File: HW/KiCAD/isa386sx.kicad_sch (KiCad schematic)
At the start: 174 parts, among them CON1 CF-CARD-cfcard, J10 PC104_16, J11 PC104, J12 USB_B, J13 POWER 5V2A, J14 COM1, J15 COM2, J16 ESP, J17 Mini-DIN-6, J18 Mini-DIN-6, J9 Conn_01x04, Q1 BC817, Q2 BC856, Q3 BC856, SW1 Jumper / Pin header 1x2 Pitch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, SW2 SW_Push, SW3 SW_DIP_x01, U10 74HCT32PW, U11 MSM5118160F-JS, U12 74HCT138PW, U13 ST16C554D, U14 74HCT138PW, U15 GD75232PW, U16 GD75232PW, U17 MAX809LEUR, U18 CH340G, U19 LMR62014, U20 ESP-12F, U21 IP4220CZ6, U22 IP4220CZ6, U23 1117-3.3, U24 ICL7660A, U25 39SF040, U26 TXS0104PW, U6 MSM5118160F-JS, U7 M6117D, U8 MSM5118160F-JS, U9 MSM5118160F-JS, X1 14.318 MHz, X2 80 MHz, X3 1.8432 Mhz, Y3 32768 Hz, Y4 12 MHz

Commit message: some edit
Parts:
- BT1: footprint my:CR2032V -> Battery:BatteryHolder_MYOUNG_BS-07-A1BJ001_CR2032
- C102, C103, C98: footprint Capacitor_Tantalum_SMD:CP_EIA-3528-21_Kemet-B_Pad1.50x2.35mm_HandSolder -> Capacitor_Tantalum_SMD:CP_EIA-3528-21_Kemet-B_HandSolder
- C75: footprint Capacitor_Tantalum_SMD:CP_EIA-7343-31_Kemet-D_Pad2.25x2.55mm_HandSolder -> Capacitor_Tantalum_SMD:CP_EIA-7343-31_Kemet-D_HandSolder
- CON1: footprint my:TE_1734451-1-LONG -> Library:TE_1734451-1
- H1, H2, H3, H4: footprint my:MountingHole_3.2mm_M3_dk5.2mm_Mask -> Library_user:MountingHole_3.2mm_M3_dk5.2mm_Mask
- J17, J18: footprint my:minidin-6 -> Library_user:minidin-6
- LOGO1: footprint mygraphic:black-mage-12.5x8.6 -> Library_user:black-mage-12.5x8.6
- U11, U6, U8, U9: footprint my:SOJ-42 -> Library_user:SOJ-42
- U25: footprint my:PLCC-32_11.4x14.0mm_P1.27mm-longpads -> Library_user:PLCC-32_11.4x14.0mm_P1.27mm-longpads
- X1, X2: footprint my:Oscillator_SMD_7050_7.0x5.0mm -> Oscillator:Oscillator_SMD_Abracon_ASE-4Pin_3.2x2.5mm_HandSoldering
- X3: footprint my:Oscillator_SMD_7050_7.0x5.0mm -> Oscillator:Oscillator_SMD_Abracon_ASV-4Pin_7.0x5.1mm_HandSoldering
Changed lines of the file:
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@@
 			)
 		)
-		(property "Footprint" "my:TE_1734451-1-LONG"
+		(property "Footprint" "Library:TE_1734451-1"
 			(at 233.172 69.85 0)
 			(effects
@@
 			)
 		)
-		(property "Footprint" "my:PLCC-32_11.4x14.0mm_P1.27mm-longpads"
+		(property "Footprint" "Library_user:PLCC-32_11.4x14.0mm_P1.27mm-longpads"
 			(at 542.29 236.22 0)
 			(effects
@@
 			)
 		)
-		(property "Footprint" "Capacitor_Tantalum_SMD:CP_EIA-7343-31_Kemet-D_Pad2.25x2.55mm_HandSolder"
+		(property "Footprint" "Capacitor_Tantalum_SMD:CP_EIA-7343-31_Kemet-D_HandSolder"
 			(at 411.1752 -17.78 0)
 			(effects
@@
 			)
 		)
-		(property "Footprint" "my:CR2032V"
+		(property "Footprint" "Battery:BatteryHolder_MYOUNG_BS-07-A1BJ001_CR2032"
 			(at 566.42 40.386 90)
 			(effects
@@
 			)
 		)
-		(property "Footprint" "my:SOJ-42"
+		(property "Footprint" "Library_user:SOJ-42"
 			(at 137.16 358.14 0)
 			(effects
@@
 			)
 		)
-		(property "Footprint" "my:MountingHole_3.2mm_M3_dk5.2mm_Mask"
+		(property "Footprint" "Library_user:MountingHole_3.2mm_M3_dk5.2mm_Mask"
 			(at 552.45 293.37 0)
 			(effects
@@
 			)
 		)
-		(property "Footprint" "my:MountingHole_3.2mm_M3_dk5.2mm_Mask"
+		(property "Footprint" "Library_user:MountingHole_3.2mm_M3_dk5.2mm_Mask"
 			(at 552.45 298.45 0)
 			(effects
@@
 			)
 		)
-		(property "Footprint" "my:MountingHole_3.2mm_M3_dk5.2mm_Mask"
+		(property "Footprint" "Library_user:MountingHole_3.2mm_M3_dk5.2mm_Mask"
 			(at 552.45 303.53 0)
 			(effects
@@
 			)
 		)
-		(property "Footprint" "my:Oscillator_SMD_7050_7.0x5.0mm"
+		(property "Footprint" "Oscillator:Oscillator_SMD_Abracon_ASE-4Pin_3.2x2.5mm_HandSoldering"
 			(at 233.68 223.52 0)
 			(effects
@@
 			)
 		)
-		(property "Footprint" "Capacitor_Tantalum_SMD:CP_EIA-3528-21_Kemet-B_Pad1.50x2.35mm_HandSolder"
+		(property "Footprint" "Capacitor_Tantalum_SMD:CP_EIA-3528-21_Kemet-B_HandSolder"
 			(at 563.5752 90.17 0)
 			(effects
@@
 			)
 		)
-		(property "Footprint" "my:minidin-6"
+		(property "Footprint" "Library_user:minidin-6"
 			(at 560.07 171.45 0)
 			(effects
@@
 			)
 		)
-		(property "Footprint" "my:minidin-6"
+		(property "Footprint" "Library_user:minidin-6"
 			(at 560.07 133.35 0)
 			(effects
@@
 			)
 		)
-		(property "Footprint" "Capacitor_Tantalum_SMD:CP_EIA-3528-21_Kemet-B_Pad1.50x2.35mm_HandSolder"
+		(property "Footprint" "Capacitor_Tantalum_SMD:CP_EIA-3528-21_Kemet-B_HandSolder"
 			(at 540.7152 39.37 0)
 			(effects
@@
 			)
 		)
-		(property "Footprint" "my:MountingHole_3.2mm_M3_dk5.2mm_Mask"
+		(property "Footprint" "Library_user:MountingHole_3.2mm_M3_dk5.2mm_Mask"
 			(at 552.45 288.29 0)
 			(effects
@@
 			)
 		)
-		(property "Footprint" "my:Oscillator_SMD_7050_7.0x5.0mm"
+		(property "Footprint" "Oscillator:Oscillator_SMD_Abracon_ASE-4Pin_3.2x2.5mm_HandSoldering"
 			(at 233.68 199.39 0)
 			(effects
@@
 			)
 		)
-		(property "Footprint" "my:SOJ-42"
+		(property "Footprint" "Library_user:SOJ-42"
 			(at 260.35 358.14 0)
 			(effects
@@
 			)
 		)
-		(property "Footprint" "my:SOJ-42"
+		(property "Footprint" "Library_user:SOJ-42"
 			(at 73.66 358.14 0)
 			(effects
@@
 			)
 		)
-		(property "Footprint" "Capacitor_Tantalum_SMD:CP_EIA-3528-21_Kemet-B_Pad1.50x2.35mm_HandSolder"
+		(property "Footprint" "Capacitor_Tantalum_SMD:CP_EIA-3528-21_Kemet-B_HandSolder"
 			(at 555.9552 97.79 0)
 			(effects
@@
 			)
 		)
-		(property "Footprint" "my:Oscillator_SMD_7050_7.0x5.0mm"
+		(property "Footprint" "Oscillator:Oscillator_SMD_Abracon_ASV-4Pin_7.0x5.1mm_HandSoldering"
 			(at 309.88 276.86 0)
 			(effects
@@
 			)
 		)
-		(property "Footprint" "my:SOJ-42"
+		(property "Footprint" "Library_user:SOJ-42"
 			(at 196.85 358.14 0)
 			(effects
@@
 			)
 		)
-		(property "Footprint" "mygraphic:black-mage-12.5x8.6"
+		(property "Footprint" "Library_user:black-mage-12.5x8.6"
 			(at 523.24 301.625 0)
 			(effects

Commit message: pcb edit
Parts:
- removed RN1, RN2, RN3, RN4: 4.7k, Resistor_SMD:R_Array_Convex_4x0603, symbol Device:R_Pack04
- removed RN5, RN6: 330, Resistor_SMD:R_Array_Convex_4x0603, symbol Device:R_Pack04
- removed RN7: 1k, Resistor_SMD:R_Array_Convex_4x0603, symbol Device:R_Pack04
- added R100, R101, R102, R103, R104, R105, R106, R107, R108, R109, R110, R111, R112, R113, R114, R115, R116, R117, R88, R93, R94, R95, R96, R97, R98, R99: 4.7k, Resistor_SMD:R_0805_2012Metric_Pad1.20x1.40mm_HandSolder, symbol Device:R
- C100, C101, C29, C30, C31, C33, C34, C35, C36, C37, C38, C39, C40, C41, C42, C43, C44, C45, C46, C47, C48, C49, C50, C51, C52, C53, C54, C55, C56, C57, C58, C59, C60, C61, C62, C63, C64, C65, C66, C67, C68, C69, C71, C73, C76, C77, C79, C80, C81, C82, C83, C85, C86, C87, C88, C90, C91, C92, C96, C97, C99: footprint Capacitor_SMD:C_0603_1608Metric_Pad1.08x0.95mm_HandSolder -> Capacitor_SMD:C_0805_2012Metric_Pad1.18x1.45mm_HandSolder
- L4: footprint Inductor_SMD:L_Taiyo-Yuden_NR-60xx_HandSoldering -> Inductor_SMD:L_Panasonic_PCC-M0850M
- R24, R25, R26, R27, R28, R29, R31, R32, R33, R34, R35, R36, R37, R38, R39, R40, R43, R44, R45, R46, R47, R48, R49, R50, R51, R52: footprint Resistor_SMD:R_0603_1608Metric_Pad0.98x0.95mm_HandSolder -> Resistor_SMD:R_0805_2012Metric_Pad1.20x1.40mm_HandSolder
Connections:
- net +5V: now also R100.2, R101.2, R102.2, R103.2, R104.2, R105.2, R106.2, R107.2, R108.2, R109.2, R110.2, R111.2, R112.2, R113.2, R114.2, R115.2, R116.2, R117.2, R96.2, R97.2, R98.2, R99.2
- net GND: now also R88.1, R93.1, R94.1, R95.1
- net IOCS16: now also R111.1
- net ISA_AEN: now also R104.1
- net ISA_DACK0: now also R93.2
- net ISA_DACK1: now also R94.2
- net ISA_DACK5: now also R95.2
- net ISA_IOCHK: now also R117.1
- net ISA_IOR: now also R115.1
- net ISA_IORDY: now also R108.1
- net ISA_IOW: now also R114.1
- net ISA_MASTER: now also R110.1
- net ISA_MEMCS16: now also R116.1
- net ISA_MEMR: now also R105.1
- net ISA_MEMW: now also R106.1
- net ISA_NOWS: now also R107.1
- net ISA_REFRESH: now also R109.1
- net ISA_SD0: now also R103.1
- net ISA_SD1: now also R102.1
- net ISA_SD2: now also R101.1
- net ISA_SD3: now also R100.1
- net ISA_SD4: now also R99.1
- net ISA_SD5: now also R98.1
- net ISA_SD6: now also R97.1
- net ISA_SD7: now also R96.1
- net ISA_SMEMR: now also R113.1
- net ISA_SMEMW: now also R112.1
- net ISA_TC: now also R88.2
- no-connect marks 80 -> 78

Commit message: some eidts, remove com
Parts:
- removed C88, C91: 22p, Capacitor_SMD:C_0805_2012Metric_Pad1.18x1.45mm_HandSolder, symbol Device:C
- removed C90: 10n, Capacitor_SMD:C_0805_2012Metric_Pad1.18x1.45mm_HandSolder, symbol Device:C
- removed J14: COM1, Connector_PinHeader_2.54mm:PinHeader_2x05_P2.54mm_Vertical, symbol Connector_Generic:Conn_02x05_Odd_Even
- removed J15: COM2, Connector_PinHeader_2.54mm:PinHeader_2x05_P2.54mm_Vertical, symbol Connector_Generic:Conn_02x05_Odd_Even
- removed J16: ESP, Connector_PinHeader_2.54mm:PinHeader_2x05_P2.54mm_Vertical, symbol Connector_Generic:Conn_02x05_Odd_Even
- removed R41, R42: 22, Resistor_SMD:R_0805_2012Metric_Pad1.20x1.40mm_HandSolder, symbol Device:R
- removed R45, R46: 10k, Resistor_SMD:R_0805_2012Metric_Pad1.20x1.40mm_HandSolder, symbol Device:R
- removed unit 4 of U10
- removed unit 3 of U10
- removed U12, U14: 74HCT138PW, Package_SO:TSSOP-16_4.4x5mm_P0.65mm, symbol 74xx:74LS138
- removed U13: ST16C554D, Package_QFP:LQFP-64_10x10mm_P0.5mm, symbol my:ST16C554-LQFP
- removed U15, U16: GD75232PW, Package_SO:TSSOP-20_4.4x6.5mm_P0.65mm, symbol Interface_UART:GD75232PW
- removed U18: CH340G, Package_SO:SOIC-16_3.9x9.9mm_P1.27mm, symbol Interface_USB:CH340G
- removed U20: ESP-12F, RF_Module:ESP-12E, symbol RF_Module:ESP-12E
- removed U26: TXS0104PW, Package_SO:TSSOP-14_4.4x5mm_P0.65mm, symbol Logic_LevelTranslator:TXB0104PW
- removed X3: 1.8432 Mhz, Oscillator:Oscillator_SMD_Abracon_ASV-4Pin_7.0x5.1mm_HandSoldering, symbol Oscillator:XO91
- removed Y4: 12 MHz, Crystal:Crystal_SMD_SeikoEpson_TSX3225-4Pin_3.2x2.5mm_HandSoldering, symbol Device:Crystal_GND24
- C100: renamed from C103; footprint Capacitor_Tantalum_SMD:CP_EIA-3528-21_Kemet-B_HandSolder -> Capacitor_Tantalum_SMD:CP_EIA-3528-21_Kemet-B_Pad1.50x2.35mm_HandSolder
- C96: renamed from C75; footprint Capacitor_Tantalum_SMD:CP_EIA-7343-31_Kemet-D_HandSolder -> Capacitor_Tantalum_SMD:CP_EIA-7343-31_Kemet-D_Pad2.25x2.55mm_HandSolder
- C97: renamed from C98; footprint Capacitor_Tantalum_SMD:CP_EIA-3528-21_Kemet-B_HandSolder -> Capacitor_Tantalum_SMD:CP_EIA-7343-31_Kemet-D_Pad2.25x2.55mm_HandSolder
- C99: renamed from C102; footprint Capacitor_Tantalum_SMD:CP_EIA-3528-21_Kemet-B_HandSolder -> Capacitor_Tantalum_SMD:CP_EIA-3528-21_Kemet-B_Pad1.50x2.35mm_HandSolder
- CON1: footprint Library:TE_1734451-1 -> Library_user:TE_1734451-1-LONG
- L4: footprint Inductor_SMD:L_Panasonic_PCC-M0850M -> Inductor_SMD:L_7.3x7.3_H4.5
- renumbered C87 to C32, C96 to C36, C97 to C37, C36 to C38, C37 to C39, C38 to C40, C99 to C41, C100 to C42, C39 to C43, C40 to C44, C41 to C45, C42 to C46, C43 to C47, C44 to C48, C45 to C49, C46 to C50, C47 to C51, C48 to C52, C49 to C53, C50 to C54, C51 to C55, C52 to C56, C53 to C57, C54 to C58, C55 to C59, C56 to C60, C57 to C61, C58 to C62, C59 to C63, C60 to C64, C61 to C65, C62 to C66, C63 to C67, C64 to C68, C65 to C69, C66 to C70, C32 to C71, C67 to C72, C68 to C73, C69 to C74, C70 to C75, C71 to C76, C72 to C77, C73 to C78, C74 to C79, C76 to C80, C77 to C81, C78 to C82, C79 to C83, C80 to C84, C81 to C85, C82 to C86, C83 to C87, C84 to C88, C85 to C89, C86 to C90, C89 to C91, C101 to C98, D6 to D4, D7 to D5, D8 to D6, D4 to D7, D5 to D8, J17 to J11, J18 to J12, J11 to J13, J12 to J14, J13 to J15, Q3 to Q2, Q2 to Q3, R88 to R25, R93 to R26, R94 to R27, R95 to R28, R25 to R29, R26 to R30, R27 to R31, R28 to R32, R96 to R33, R97 to R34, R98 to R35, R99 to R36, R100 to R37, R101 to R38, R102 to R39, R103 to R40, R104 to R41, R105 to R42, R106 to R43, R107 to R44, R108 to R45, R109 to R46, R110 to R47, R111 to R48, R112 to R49, R113 to R50, R114 to R51, R115 to R52, R116 to R53, R117 to R54, R29 to R55, R30 to R56, R38 to R57, R31 to R58, R40 to R59, R48 to R60, R49 to R61, R50 to R62, R51 to R63, R52 to R64, R32 to R65, R34 to R66, R35 to R67, R36 to R68, R39 to R69, R43 to R70, R44 to R71, R33 to R72, R47 to R73, R37 to R74, SW2 to SW1, SW3 to SW2, SW1 to SW3, U17 to U11, U11 to U12, U21 to U13, U22 to U14, U25 to U15, U19 to U16, U23 to U17, U24 to U18
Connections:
- no-connect marks 78 -> 51
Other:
- note removed: "19mA"
- note removed: "215mA"
- note removed: "30mA"
- note removed: "6mA"
- note removed: "COM (UART)"
- note removed: "COM1 (C): I/O port 0x3F8, IRQ 4 COM2 (D): I/O port 0x2F8, IRQ 3 COM3 (B): I/O port 0x3E8, IRQ 4 - USB COM4 (A): I/O port 0x2E8, IRQ 3 - WiFi"
- note removed: "Pull ESP_BOOT to GND to enter programming mode."
- note removed: "WiFi"
- moved on the sheet: C32, C36, C37, C41, C42, C71, C96, D1, D2, D3, D7, D8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

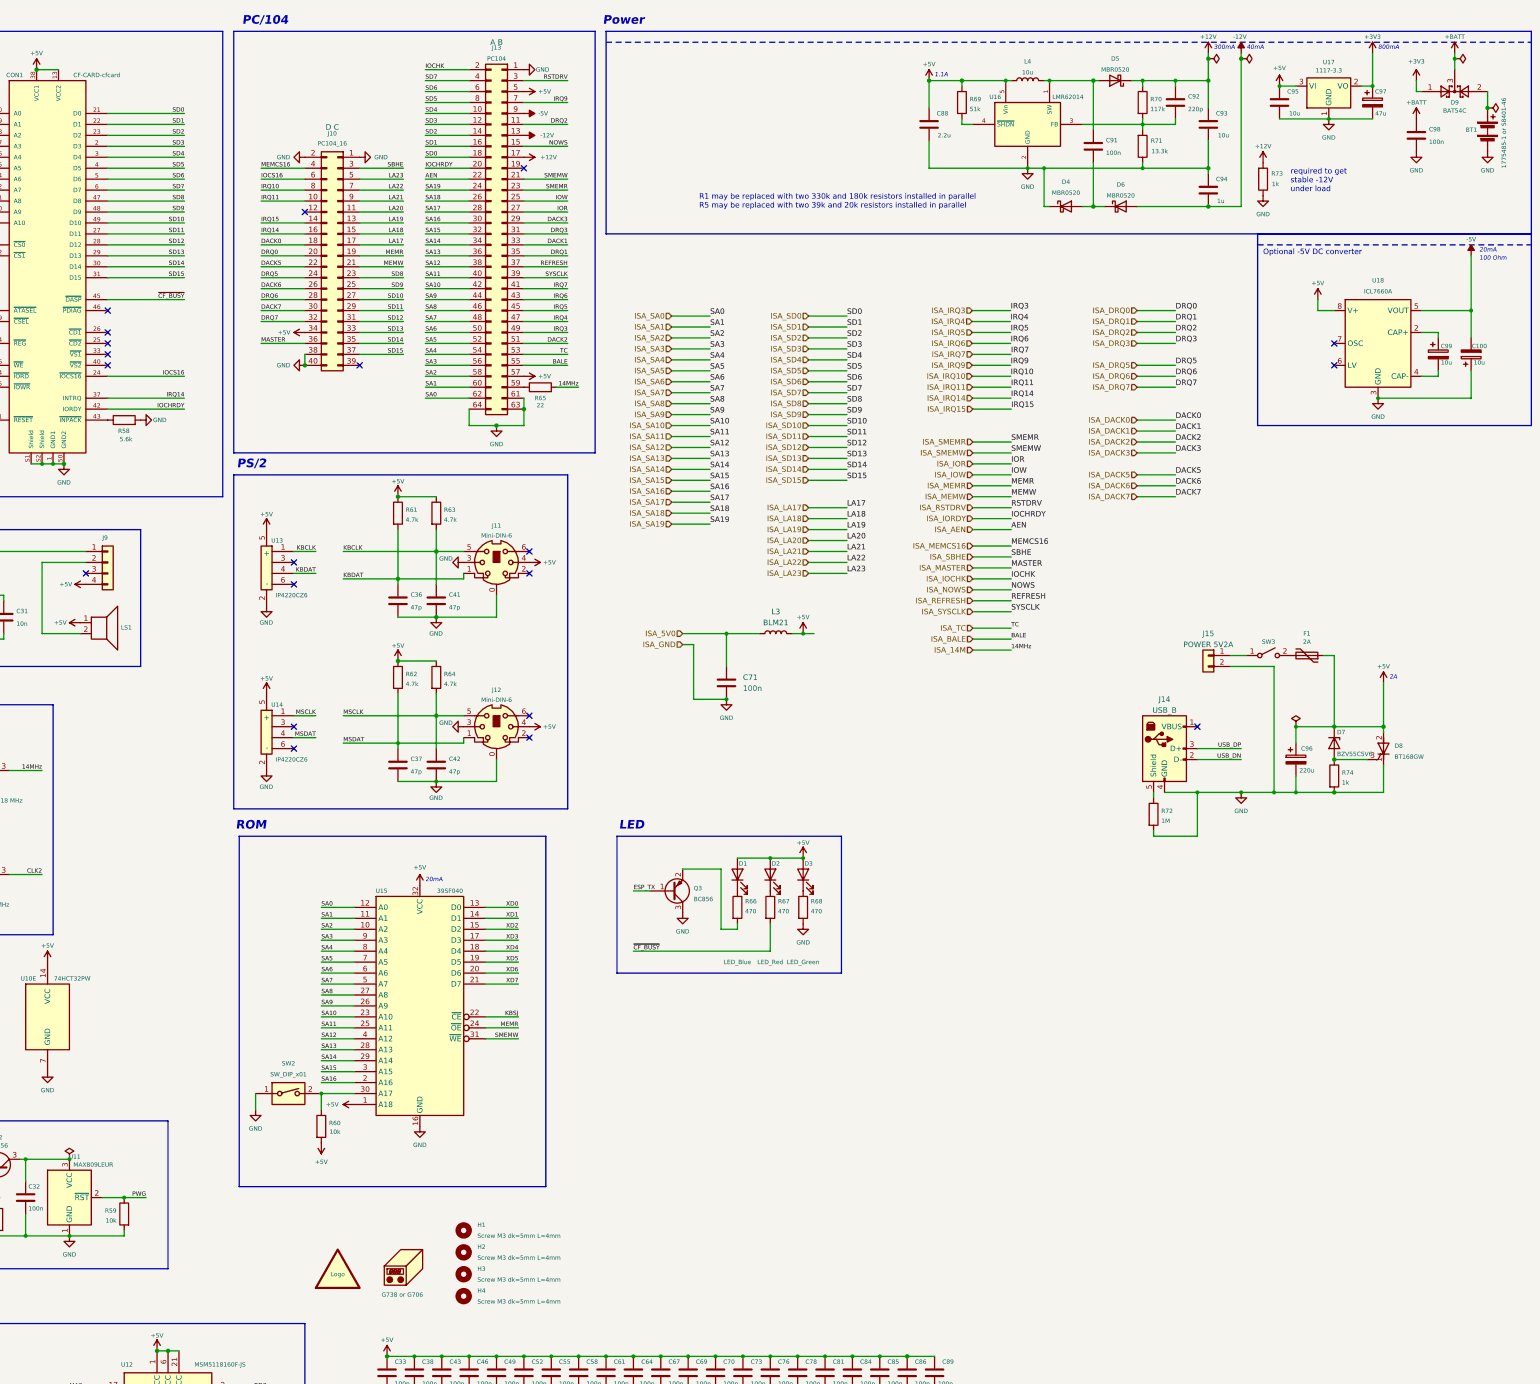
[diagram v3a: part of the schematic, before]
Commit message: some edits, add HP amp
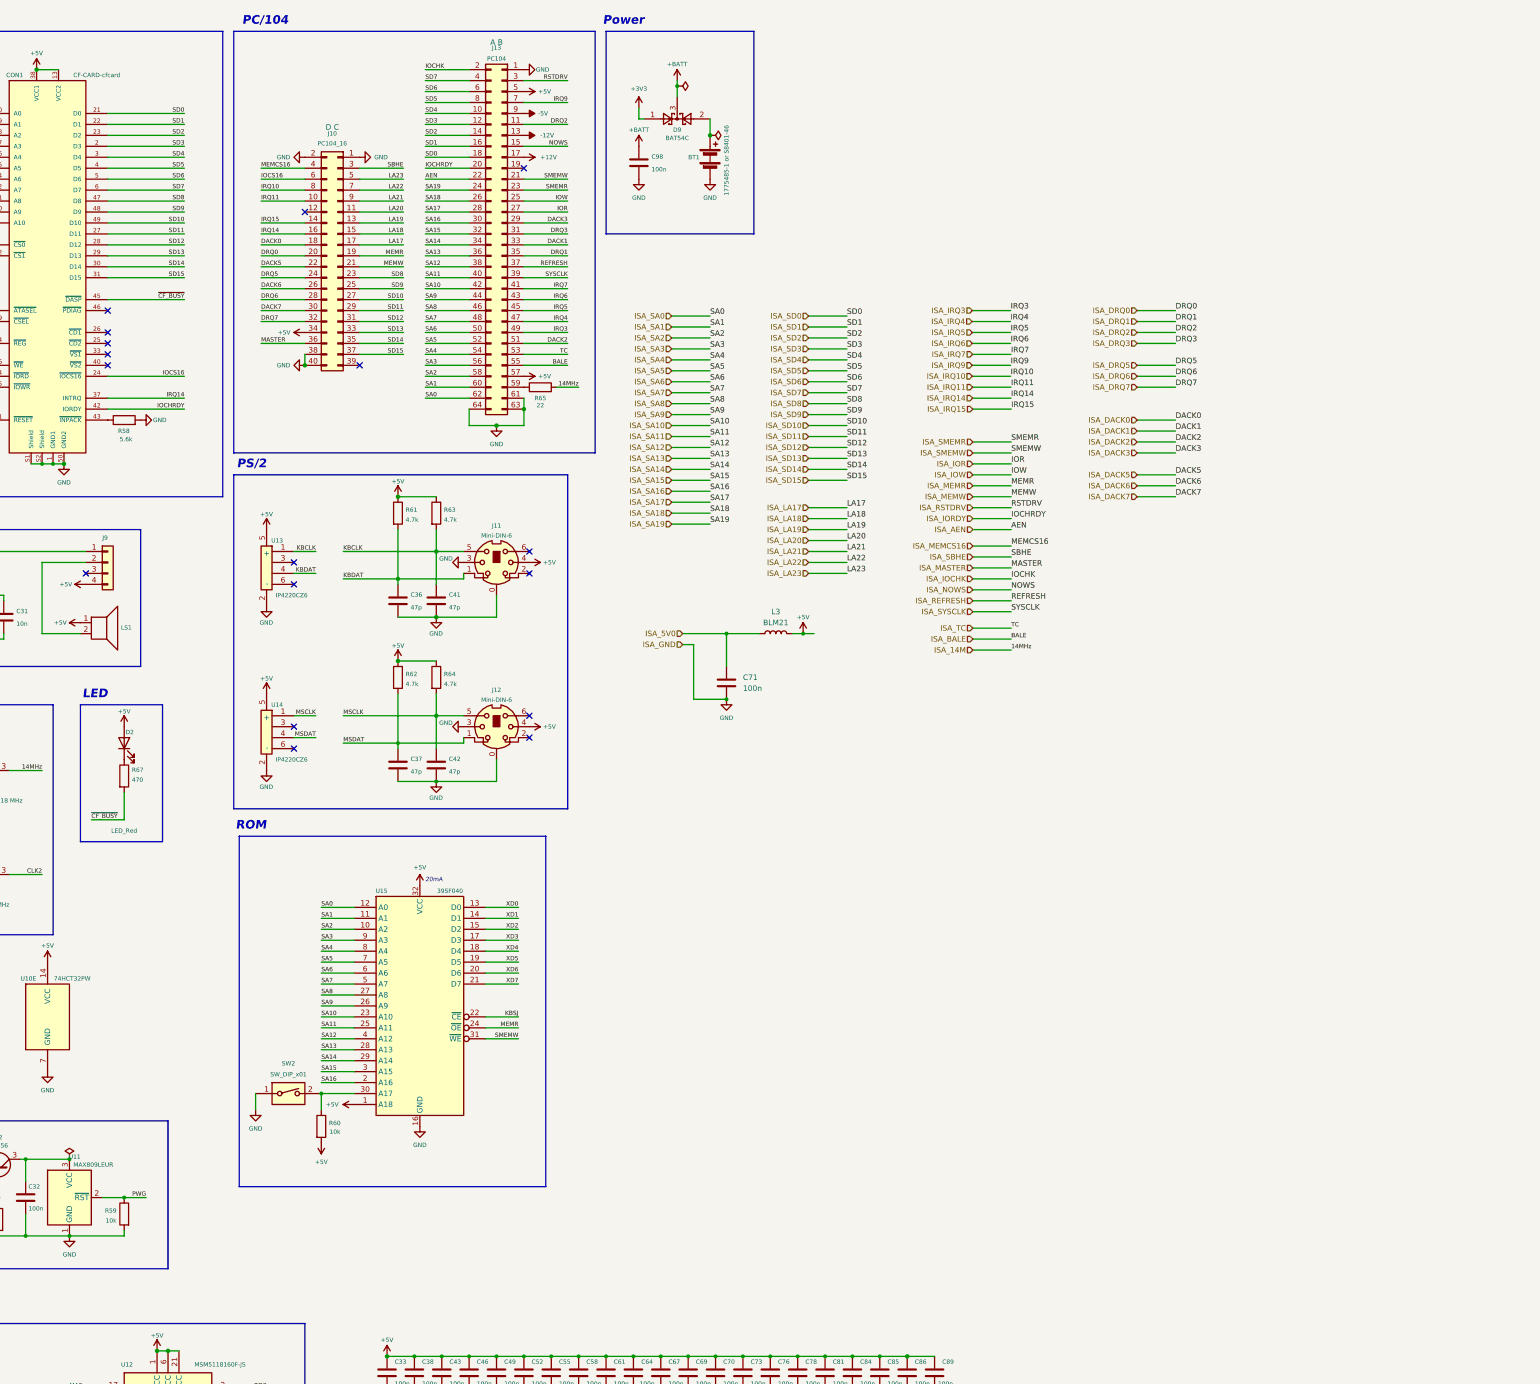
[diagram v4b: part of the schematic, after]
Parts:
- removed C100, C99: 10u, Capacitor_Tantalum_SMD:CP_EIA-3528-21_Kemet-B_Pad1.50x2.35mm_HandSolder, symbol Device:C_Polarized
- removed C88: 2.2u, Capacitor_SMD:C_0805_2012Metric_Pad1.18x1.45mm_HandSolder, symbol Device:C
- removed C91: 100n, Capacitor_SMD:C_0805_2012Metric_Pad1.18x1.45mm_HandSolder, symbol Device:C
- removed C92: 220p, Capacitor_SMD:C_0805_2012Metric_Pad1.18x1.45mm_HandSolder, symbol Device:C
- removed C93, C95: 10u, Capacitor_SMD:C_0805_2012Metric_Pad1.18x1.45mm_HandSolder, symbol Device:C
- removed C94: 1u, Capacitor_SMD:C_0805_2012Metric_Pad1.18x1.45mm_HandSolder, symbol Device:C
- removed C96: 220u, Capacitor_Tantalum_SMD:CP_EIA-7343-31_Kemet-D_Pad2.25x2.55mm_HandSolder, symbol Device:C_Polarized
- removed C97: 47u, Capacitor_Tantalum_SMD:CP_EIA-7343-31_Kemet-D_Pad2.25x2.55mm_HandSolder, symbol Device:C_Polarized
- removed D1: LED_Blue, LED_THT:LED_D3.0mm_Horizontal_O1.27mm_Z6.0mm, symbol Device:LED
- removed D3: LED_Green, LED_THT:LED_D3.0mm_Horizontal_O1.27mm_Z6.0mm, symbol Device:LED
- removed D4, D5, D6: MBR0520, Diode_SMD:D_SOD-123, symbol Diode:MBR0520
- removed D7: BZV55C5V6, Diode_SMD:D_MiniMELF, symbol Device:D_Zener
- removed D8: BT168GW, Package_TO_SOT_SMD:SOT-223-3_TabPin2, symbol Device:Q_SCR_KAG
- removed F1: 2A, Fuse:Fuse_1812_4532Metric_Pad1.30x3.40mm_HandSolder, symbol Device:Polyfuse
- removed H1, H2, H3, H4: Screw M3 dk=5mm L=4mm, Library_user:MountingHole_3.2mm_M3_dk5.2mm_Mask, symbol Mechanical:MountingHole
- removed J14: USB_B, Connector_USB:USB_B_Lumberg_2411_02_Horizontal, symbol Connector:USB_B
- removed J15: POWER 5V2A, TerminalBlock:TerminalBlock_bornier-2_P5.08mm, symbol Connector_Generic:Conn_01x02
- removed L4: 10u, Inductor_SMD:L_7.3x7.3_H4.5, symbol Device:L
- removed LOGO1: graphic, Library_user:black-mage-12.5x8.6, symbol my:logo
- removed N1: G738 or G706, my:G738, symbol Mechanical:Housing
- removed Q3: BC856, Package_TO_SOT_SMD:SOT-23, symbol Transistor_BJT:BC856
- removed R66, R68: 470, Resistor_SMD:R_0805_2012Metric_Pad1.20x1.40mm_HandSolder, symbol Device:R
- removed R69: 51k, Resistor_SMD:R_0805_2012Metric_Pad1.20x1.40mm_HandSolder, symbol Device:R
- removed R70: 117k, Resistor_SMD:R_0805_2012Metric_Pad1.20x1.40mm_HandSolder, symbol Device:R
- removed R71: 13.3k, Resistor_SMD:R_0805_2012Metric_Pad1.20x1.40mm_HandSolder, symbol Device:R
- removed R72: 1M, Resistor_SMD:R_0805_2012Metric_Pad1.20x1.40mm_HandSolder, symbol Device:R
- removed R73, R74: 1k, Resistor_SMD:R_0805_2012Metric_Pad1.20x1.40mm_HandSolder, symbol Device:R
- removed SW3: Jumper / Pin header 1x2 Pitch=2.54mm, Connector_Molex:Molex_KK-254_AE-6410-02A_1x02_P2.54mm_Vertical, symbol Switch:SW_SPST
- removed U16: LMR62014, Package_TO_SOT_SMD:SOT-23-5_HandSoldering, symbol my:LT1930
- removed U17: 1117-3.3, Package_TO_SOT_SMD:SOT-223-3_TabPin2, symbol Regulator_Linear:AMS1117-3.3
- removed U18: ICL7660A, Package_SO:SOIC-8_3.9x4.9mm_P1.27mm, symbol Regulator_SwitchedCapacitor:ICL7660
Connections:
- no-connect marks 51 -> 48
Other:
- note removed: "1.1A"
- note removed: "100 Ohm"
- note removed: "2A"
- note removed: "300mA"
- note removed: "40mA"
- note removed: "800mA"
- note removed: "Optional -5V DC converter"
- note removed: "R1 may be replaced with two 330k and 180k resistors installed in parallel R5 may be replaced with two 39k and 20k resistors installed in parallel"
- note removed: "required to get stable -12V under load"
- moved on the sheet: BT1, C98, D2, D9, R67
